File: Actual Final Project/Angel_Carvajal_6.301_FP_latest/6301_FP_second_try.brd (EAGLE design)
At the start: 101.6 x 50.8 mm, 16 parts, among them IC1 MPQ3904, IC2 MPQ3906, IC3 TL072P, IC4 CD4066BE, IC5 LM311N

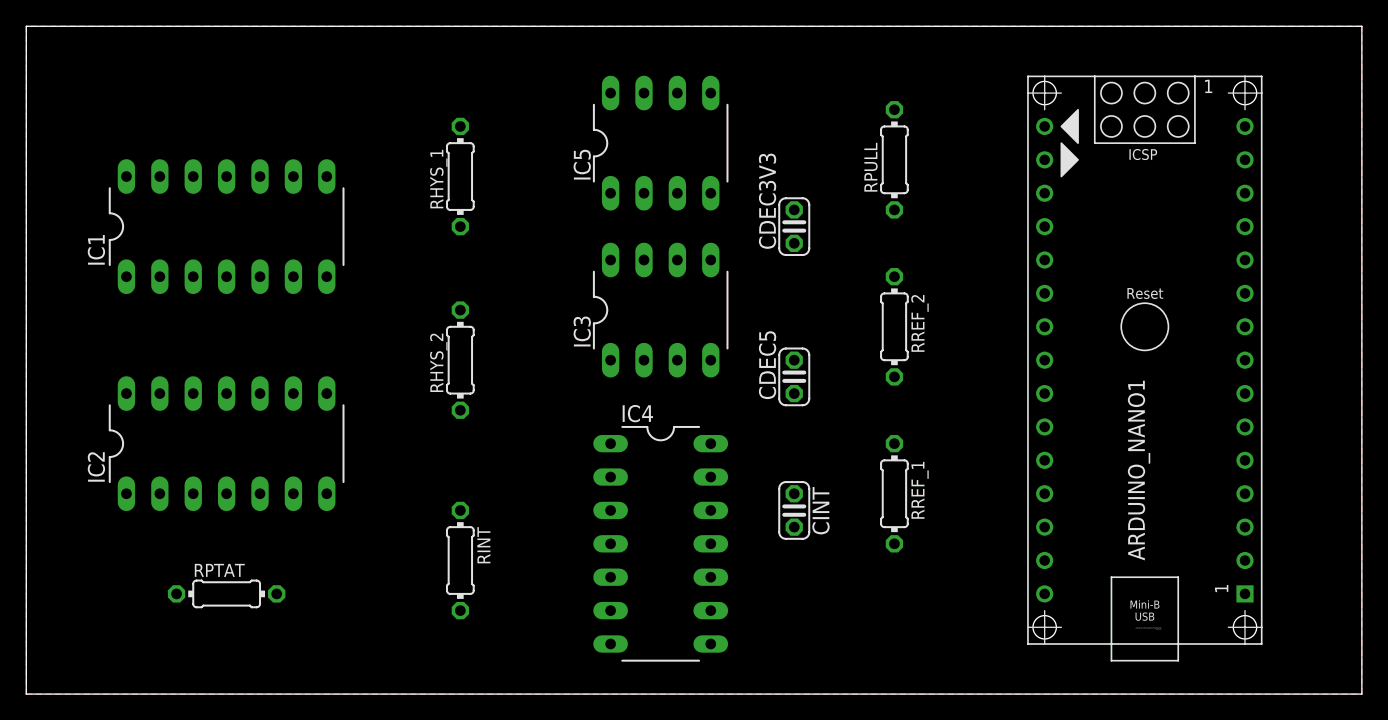
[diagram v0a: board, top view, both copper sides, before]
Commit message: PCB3_DONE
-Still get errors from DRC: Dimension from Arduino/Via Drill sizes
-Got the 2nd Layer in though
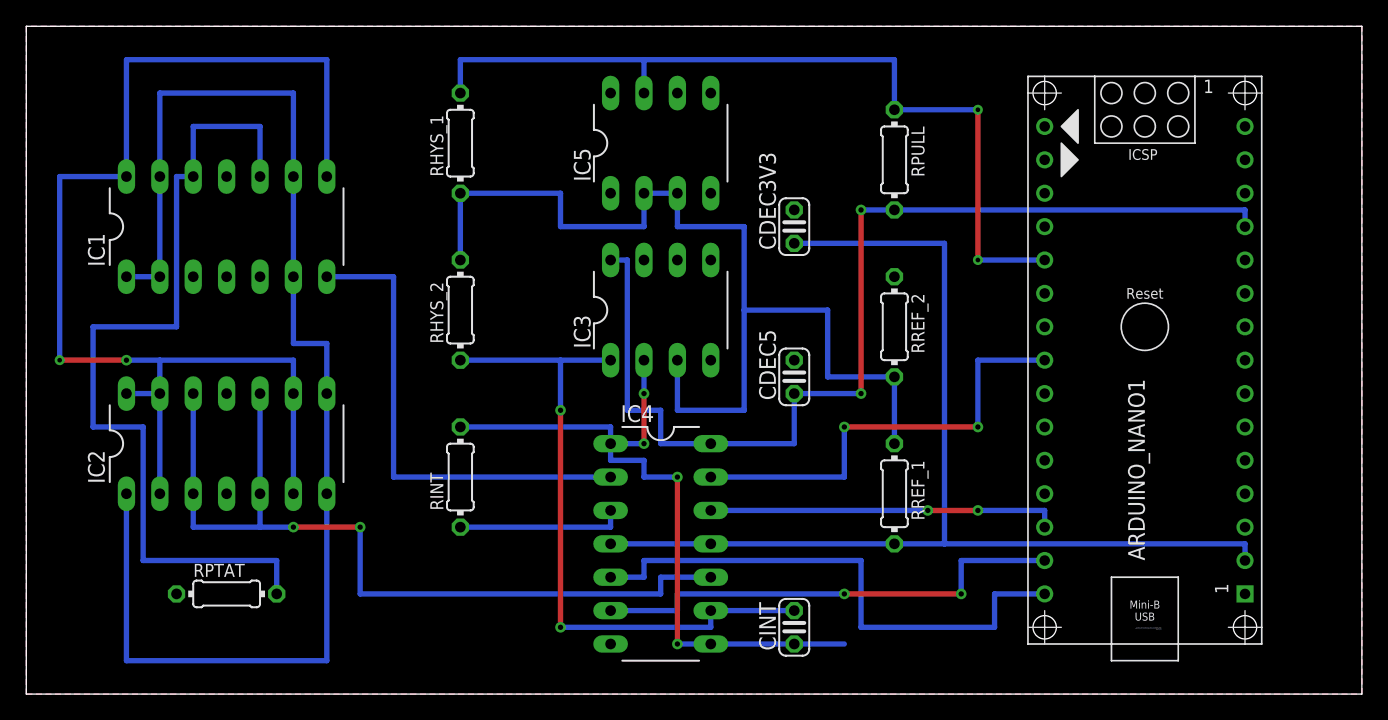
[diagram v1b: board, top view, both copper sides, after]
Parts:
- moved CINT 8.89 mm to (58.4, 5.08), turned to 90 degrees
- moved RINT 6.35 mm to (33.0, 16.5), turned to 90 degrees
- moved RHYS_2 3.81 mm to (33.0, 29.2)
- moved RHYS_1 2.54 mm to (33.0, 41.9)
- turned RPULL to 270 degrees
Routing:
- net N$5: track 0.00 -> 100.3 mm
- net N$3: track 0.00 -> 92.7 mm, vias 0 -> 2
- net 3V3: track 0.00 -> 83.8 mm
- net 5V: track 0.00 -> 81.3 mm, vias 0 -> 2
- net VREF: track 0.00 -> 78.7 mm
- net START: track 0.00 -> 66.0 mm, vias 0 -> 2
- net N$2: track 0.00 -> 66.0 mm
- net N$4: track 0.00 -> 64.8 mm, vias 0 -> 2
- net N$10: track 0.00 -> 54.6 mm, vias 0 -> 4
- net N$6: track 0.00 -> 50.8 mm, vias 0 -> 2
- net SW_B: track 0.00 -> 41.9 mm
- net SW_C: track 0.00 -> 36.8 mm, vias 0 -> 2
- net N$9: track 0.00 -> 36.8 mm
- net SW_A: track 0.00 -> 34.3 mm, vias 0 -> 2
- net SW_D: track 0.00 -> 26.7 mm, vias 0 -> 2
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- added copper zone on layer 16, net GND
